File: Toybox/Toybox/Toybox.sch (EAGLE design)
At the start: 13 parts, among them J1 RASPBERRYPI-40-PIN-GPIO, X1 USB-A-TH

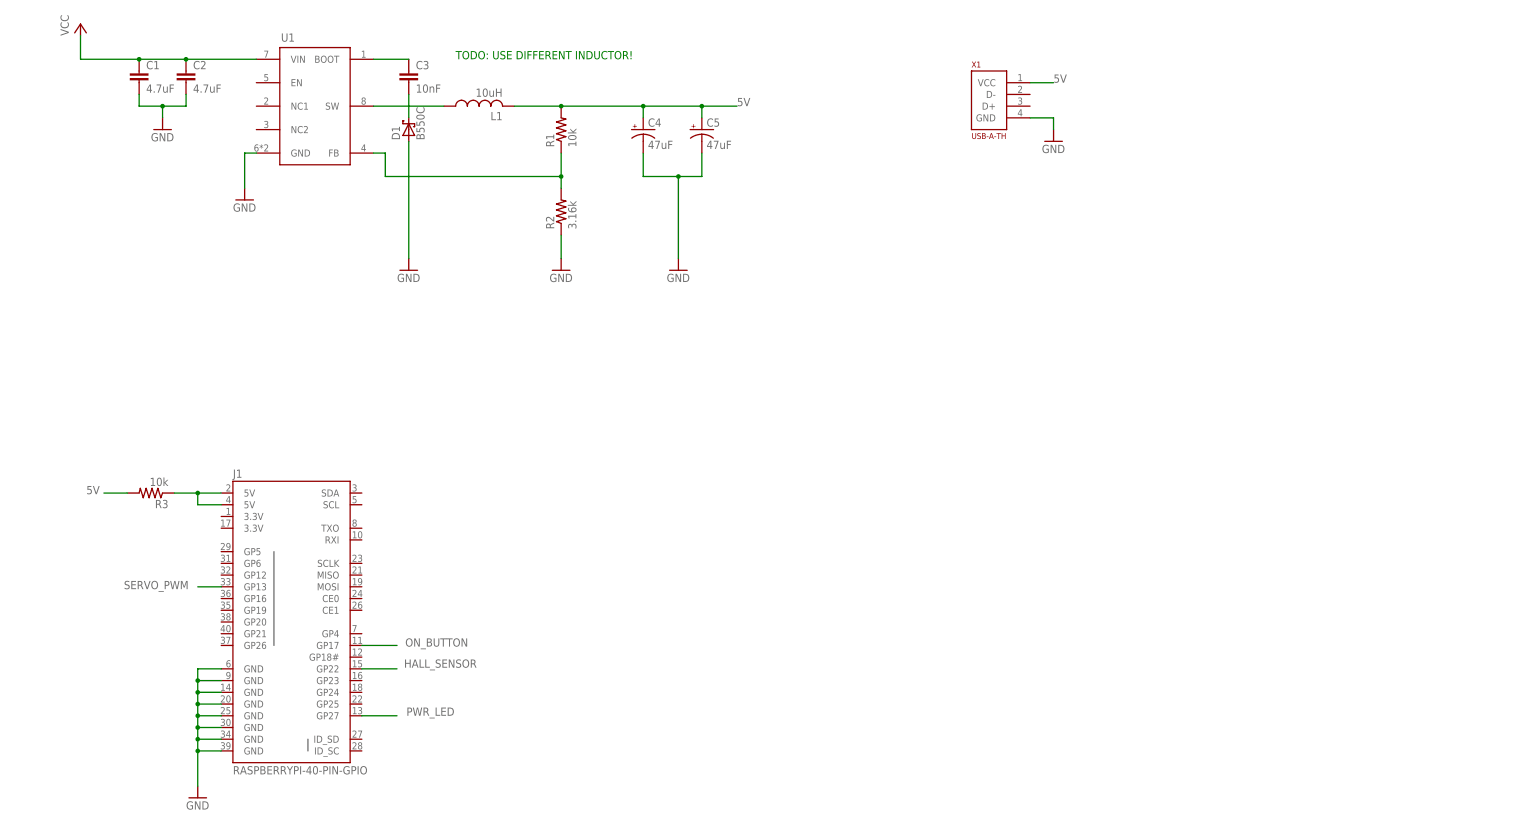
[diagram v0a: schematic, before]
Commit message: Circuit is mostly done. Just need to add the power supply terminal
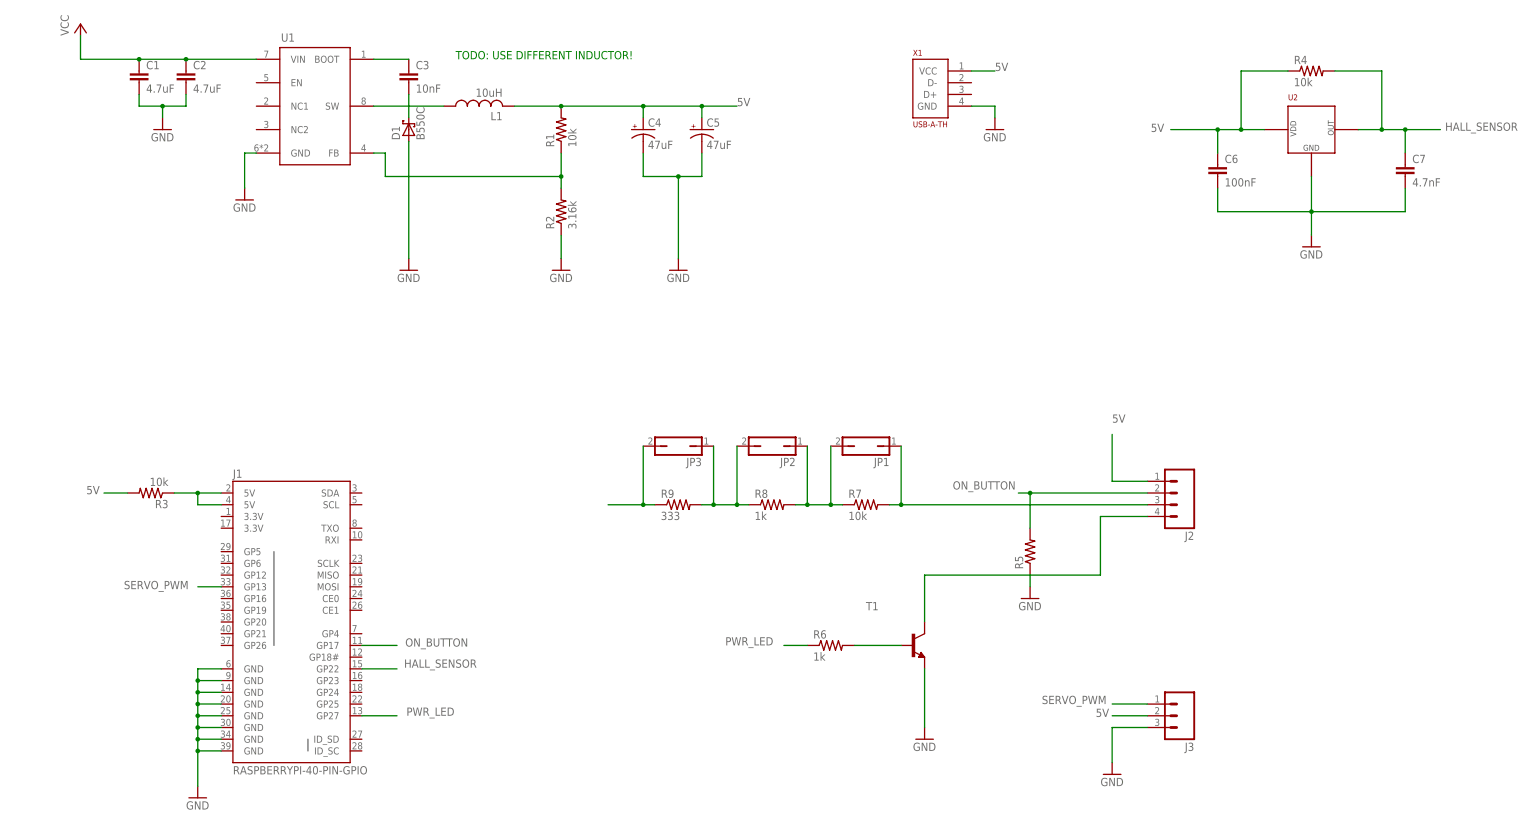
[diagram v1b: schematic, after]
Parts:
- added C6: 100nF, resistor:C-EUC0603
- added C7: 4.7nF, resistor:C-EUC0603
- added J2: (no value), SparkFun-Connectors:M041.27MM
- added J3: (no value), SparkFun-Connectors:M03PTH
- added JP1, JP2, JP3: (no value), jumper:JP1Q
- added R4, R7: 10k, resistor:R-US_R0603
- added R5: (no value), resistor:R-US_R0603
- added R6, R8: 1k, resistor:R-US_R0603
- added R9: 333, resistor:R-US_R0603
- added T1: (no value), transistor:MMBT2222ALT1-NPN-SOT23-BEC
- added U2: US1881, Toybox:US1881
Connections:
- new net N$1: J2.4, T1.C
- new net N$4: R6.2, T1.B
- new net N$7: JP2.2, JP3.1, R8.1, R9.2
- new net N$8: JP1.2, JP2.1, R7.1, R8.2
- new net N$9: J2.3, JP1.1, R7.2
- net 5V: now also C6.1, J2.1, J3.2, R4.1, U2.VDD
- net GND: now also C6.2, C7.2, J3.3, R5.1, T1.E, U2.GND
- net HALL_SENSOR: now also C7.1, R4.2, U2.OUT
- net ON_BUTTON: now also J2.2, R5.2
- net PWR_LED: now also R6.1
- net SERVO_PWM: now also J3.1
- net VCC: now also JP3.2, R9.1
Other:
- moved on the sheet: X1

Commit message: Layout is mostly complete. Need to wire small components and ground planes
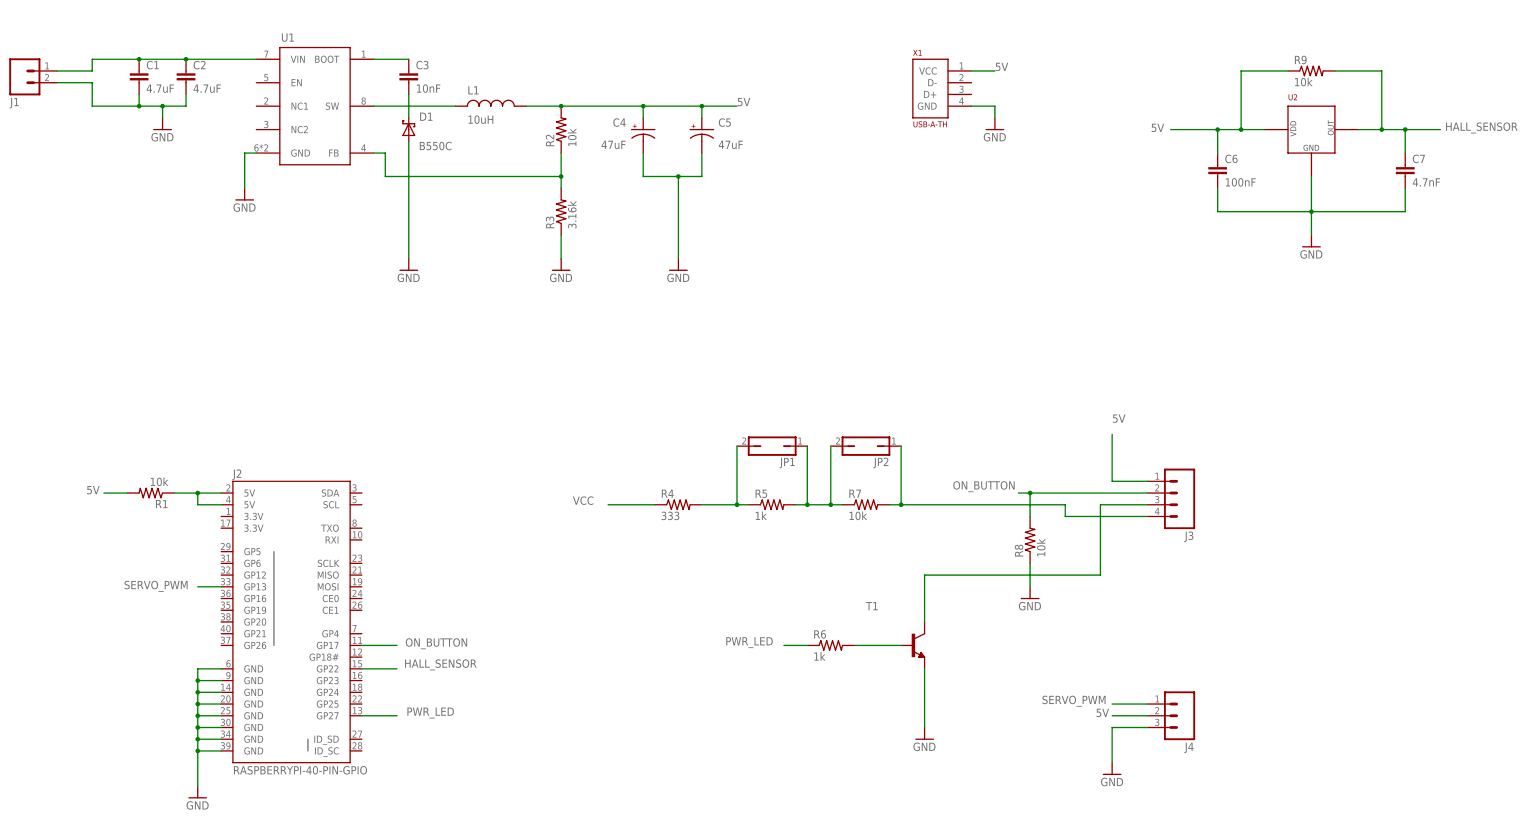
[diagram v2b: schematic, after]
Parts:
- removed JP3: (no value), jumper:JP1Q
- added J4: (no value), SparkFun-Connectors:M03PTH
- J1: value RASPBERRYPI-40-PIN-GPIO -> (none); device SparkFun-Boards:RASPBERRYPI-40-PIN-GPIO -> SparkFun-Connectors:M025MM
- J2: value (none) -> RASPBERRYPI-40-PIN-GPIO; device SparkFun-Connectors:M041.27MM -> SparkFun-Boards:RASPBERRYPI-40-PIN-GPIO
- J3: device SparkFun-Connectors:M03PTH -> SparkFun-Connectors:M04PTH
- L1: device resistor:L-USL8530M -> Toybox:SRN1060
- R2: value 3.16k -> 10k
- R3: value 10k -> 3.16k
- R4: value 10k -> 333
- R5: value (none) -> 1k
- R8: value 1k -> 10k
- R9: value 333 -> 10k
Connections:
- net 5V: now also J3.1, J4.2, R2.2, R9.1; no longer J2.1, J3.2, R3.2, R4.1
- net GND: now also J1.2, J2.GND@14, J2.GND@20, J2.GND@25, J2.GND@30, J2.GND@34, J2.GND@39, J2.GND@6, J2.GND@9, J4.3, R3.1, R8.1; no longer J1.GND@14, J1.GND@20, J1.GND@25, J1.GND@30, J1.GND@34, J1.GND@39, J1.GND@6, J1.GND@9, J3.3, R2.1, R5.1
- net HALL_SENSOR: now also J2.GP22, R9.2; no longer J1.GP22, R4.2
- net N$1: now also J3.3; no longer J2.4
- net N$2: now also J2.5V@2, J2.5V@4, R1.1; no longer J1.5V@2, J1.5V@4, R3.1
- net N$3: now also R2.1, R3.2; no longer R1.1, R2.2
- net N$7: now also JP1.2, R4.2, R5.1; no longer JP2.2, JP3.1, R8.1, R9.2
- net N$8: now also JP1.1, JP2.2, R5.2; no longer JP1.2, JP2.1, R8.2
- net N$9: now also J3.4, JP2.1; no longer J2.3, JP1.1
- net ON_BUTTON: now also J2.GP17, J3.2, R8.2; no longer J1.GP17, J2.2, R5.2
- net PWR_LED: now also J2.GP27; no longer J1.GP27
- net SERVO_PWM: now also J2.GP13, J4.1; no longer J1.GP13, J3.1
- net VCC: now also J1.1, R4.1; no longer JP3.2, R9.1
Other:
- note removed: "TODO: USE DIFFERENT INDUCTOR!"
- moved on the sheet: JP1, JP2, R1, R2, R3, R4, R5, R8, R9

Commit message: Circuit is complete. Add logo if there is time
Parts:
- removed U2: US1881, Toybox:US1881
- added J5: (no value), SparkFun-Connectors:M03PTH
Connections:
- new net NC1: J2.3.3V@1
- new net NC2: J2.3.3V@17
- net 5V: now also J5.1, R9.2; no longer R9.1, U2.VDD
- net GND: now also J5.3; no longer U2.GND
- net HALL_SENSOR: now also J5.2, R9.1; no longer R9.2, U2.OUT
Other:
- moved on the sheet: C6, C7, R9
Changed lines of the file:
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@@
 <part name="R1" library="resistor" deviceset="R-US_" device="R0603" value="10k"/>
 <part name="GND2" library="supply1" deviceset="GND" device=""/>
-<part name="U2" library="Toybox" deviceset="US1881" device=""/>
 <part name="C6" library="resistor" deviceset="C-EU" device="C0603" value="100nF"/>
 <part name="C7" library="resistor" deviceset="C-EU" device="C0603" value="4.7nF"/>
@@
 <part name="J3" library="SparkFun-Connectors" deviceset="M04" device="PTH"/>
 <part name="J4" library="SparkFun-Connectors" deviceset="M03" device="PTH"/>
+<part name="J5" library="SparkFun-Connectors" deviceset="M03" device="PTH"/>
 </parts>
 <sheets>
@@
 <instance part="R1" gate="G$1" x="30.48" y="63.5" rot="R180"/>
 <instance part="GND2" gate="1" x="40.64" y="-2.54"/>
-<instance part="U2" gate="G$1" x="281.94" y="142.24"/>
-<instance part="C6" gate="G$1" x="261.62" y="134.62"/>
-<instance part="C7" gate="G$1" x="302.26" y="134.62"/>
-<instance part="R9" gate="G$1" x="281.94" y="154.94"/>
-<instance part="GND11" gate="1" x="281.94" y="116.84"/>
+<instance part="C6" gate="G$1" x="276.86" y="116.84"/>
+<instance part="C7" gate="G$1" x="289.56" y="101.6"/>
+<instance part="R9" gate="G$1" x="289.56" y="116.84" smashed="yes" rot="R90">
+<attribute name="NAME" x="294.894" y="119.6594" size="1.778" layer="95" rot="R180"/>
+<attribute name="VALUE" x="295.91" y="115.062" size="1.778" layer="96" rot="R180"/>
+</instance>
+<instance part="GND11" gate="1" x="289.56" y="83.82"/>
 <instance part="R8" gate="G$1" x="220.98" y="53.34" rot="R90"/>
 <instance part="GND9" gate="1" x="220.98" y="40.64"/>
@@
 <instance part="J3" gate="G$1" x="251.46" y="63.5" rot="R180"/>
 <instance part="J4" gate="J$1" x="254" y="15.24" rot="R180"/>
+<instance part="J5" gate="J$1" x="309.88" y="106.68" rot="R180"/>
 </instances>
 <busses>
@@
 </segment>
 <segment>
-<pinref part="C6" gate="G$1" pin="2"/>
-<wire x1="261.62" y1="129.54" x2="261.62" y2="124.46" width="0.1524" layer="91"/>
-<pinref part="C7" gate="G$1" pin="2"/>
-<wire x1="261.62" y1="124.46" x2="281.94" y2="124.46" width="0.1524" layer="91"/>
-<wire x1="281.94" y1="124.46" x2="302.26" y2="124.46" width="0.1524" layer="91"/>
-<wire x1="302.26" y1="124.46" x2="302.26" y2="129.54" width="0.1524" layer="91"/>
-<pinref part="U2" gate="G$1" pin="GND"/>
-<wire x1="281.94" y1="132.08" x2="281.94" y2="124.46" width="0.1524" layer="91"/>
-<junction x="281.94" y="124.46"/>
-<pinref part="GND11" gate="1" pin="GND"/>
-<wire x1="281.94" y1="124.46" x2="281.94" y2="119.38" width="0.1524" layer="91"/>
-</segment>
-<segment>
 <pinref part="GND9" gate="1" pin="GND"/>
 <pinref part="R8" gate="G$1" pin="1"/>
@@
 <wire x1="198.12" y1="25.4" x2="198.12" y2="12.7" width="0.1524" layer="91"/>
 <pinref part="GND7" gate="1" pin="GND"/>
+</segment>
+<segment>
+<pinref part="C7" gate="G$1" pin="2"/>
+<pinref part="GND11" gate="1" pin="GND"/>
+<wire x1="289.56" y1="96.52" x2="289.56" y2="91.44" width="0.1524" layer="91"/>
+<wire x1="289.56" y1="91.44" x2="289.56" y2="86.36" width="0.1524" layer="91"/>
+<junction x="289.56" y="91.44"/>
+<pinref part="C6" gate="G$1" pin="2"/>
+<wire x1="276.86" y1="111.76" x2="276.86" y2="91.44" width="0.1524" layer="91"/>
+<wire x1="289.56" y1="91.44" x2="276.86" y2="91.44" width="0.1524" layer="91"/>
+<pinref part="J5" gate="J$1" pin="3"/>
+<wire x1="302.26" y1="104.14" x2="297.18" y2="104.14" width="0.1524" layer="91"/>
+<wire x1="297.18" y1="104.14" x2="297.18" y2="91.44" width="0.1524" layer="91"/>
+<wire x1="297.18" y1="91.44" x2="289.56" y2="91.44" width="0.1524" layer="91"/>
 </segment>
 </net>
@@
 </segment>
 <segment>
-<pinref part="U2" gate="G$1" pin="VDD"/>
+<wire x1="289.56" y1="132.08" x2="289.56" y2="127" width="0.1524" layer="91"/>
+<label x="292.862" y="134.112" size="1.778" layer="95"/>
+<pinref part="J5" gate="J$1" pin="1"/>
+<wire x1="302.26" y1="109.22" x2="297.18" y2="109.22" width="0.1524" layer="91"/>
+<wire x1="297.18" y1="109.22" x2="297.18" y2="127" width="0.1524" layer="91"/>
+<wire x1="297.18" y1="127" x2="289.56" y2="127" width="0.1524" layer="91"/>
+<junction x="289.56" y="127"/>
 <pinref part="C6" gate="G$1" pin="1"/>
-<wire x1="271.78" y1="142.24" x2="266.7" y2="142.24" width="0.1524" layer="91"/>
-<wire x1="266.7" y1="142.24" x2="261.62" y2="142.24" width="0.1524" layer="91"/>
-<wire x1="261.62" y1="142.24" x2="261.62" y2="137.16" width="0.1524" layer="91"/>
-<pinref part="R9" gate="G$1" pin="1"/>
-<wire x1="276.86" y1="154.94" x2="266.7" y2="154.94" width="0.1524" layer="91"/>
-<wire x1="266.7" y1="154.94" x2="266.7" y2="142.24" width="0.1524" layer="91"/>
-<junction x="266.7" y="142.24"/>
-<wire x1="261.62" y1="142.24" x2="251.46" y2="142.24" width="0.1524" layer="91"/>
-<junction x="261.62" y="142.24"/>
-<label x="247.142" y="141.732" size="1.778" layer="95"/>
+<wire x1="276.86" y1="119.38" x2="276.86" y2="127" width="0.1524" layer="91"/>
+<wire x1="276.86" y1="127" x2="289.56" y2="127" width="0.1524" layer="91"/>
+<pinref part="R9" gate="G$1" pin="2"/>
+<wire x1="289.56" y1="121.92" x2="289.56" y2="127" width="0.1524" layer="91"/>
 </segment>
 <segment>
@@
 </segment>
 <segment>
+<pinref part="J5" gate="J$1" pin="2"/>
+<wire x1="302.26" y1="106.68" x2="289.56" y2="106.68" width="0.1524" layer="91"/>
 <pinref part="C7" gate="G$1" pin="1"/>
-<wire x1="302.26" y1="137.16" x2="302.26" y2="142.24" width="0.1524" layer="91"/>
-<pinref part="U2" gate="G$1" pin="OUT"/>
-<wire x1="302.26" y1="142.24" x2="297.18" y2="142.24" width="0.1524" layer="91"/>
-<pinref part="R9" gate="G$1" pin="2"/>
-<wire x1="297.18" y1="142.24" x2="292.1" y2="142.24" width="0.1524" layer="91"/>
-<wire x1="287.02" y1="154.94" x2="297.18" y2="154.94" width="0.1524" layer="91"/>
-<wire x1="297.18" y1="154.94" x2="297.18" y2="142.24" width="0.1524" layer="91"/>
-<junction x="297.18" y="142.24"/>
-<wire x1="302.26" y1="142.24" x2="309.88" y2="142.24" width="0.1524" layer="91"/>
-<junction x="302.26" y="142.24"/>
-<label x="310.896" y="141.986" size="1.778" layer="95"/>
+<wire x1="289.56" y1="106.68" x2="269.24" y2="106.68" width="0.1524" layer="91"/>
+<wire x1="289.56" y1="106.68" x2="289.56" y2="104.14" width="0.1524" layer="91"/>
+<junction x="289.56" y="106.68"/>
+<pinref part="R9" gate="G$1" pin="1"/>
+<wire x1="289.56" y1="111.76" x2="289.56" y2="106.68" width="0.1524" layer="91"/>
+<junction x="289.56" y="106.68"/>
+<label x="268.478" y="108.204" size="1.778" layer="95" rot="R180"/>
 </segment>
 </net>
@@
 </segment>
 </net>
+<net name="NC1" class="0">
+<segment>
+<pinref part="J2" gate="G$1" pin="3.3V@1"/>
+<wire x1="45.72" y1="58.42" x2="40.64" y2="58.42" width="0.1524" layer="91"/>
+</segment>
+</net>
+<net name="NC2" class="0">
+<segment>
+<pinref part="J2" gate="G$1" pin="3.3V@17"/>
+<wire x1="45.72" y1="55.88" x2="40.64" y2="55.88" width="0.1524" layer="91"/>
+</segment>
+</net>
